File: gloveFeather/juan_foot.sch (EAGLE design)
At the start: 9 parts

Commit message: pcb for nano almost ready
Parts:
- removed FLEXPOWER, LCDSERIAL: (no value), SparkFun-Connectors:CONN_02
- removed RIGHTFLEX: (no value), SparkFun-Connectors:CONN_06LOCK
- added J1: (no value), SparkFun-Connectors:CONN_08"
- added LCD: (no value), SparkFun-Connectors:CONN_03
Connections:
- net 3V: now also J1.8; no longer FLEXPOWER.1, U$1.3.3V
- net GND: now also J1.7, LCD.3; no longer FLEXPOWER.2
- net PINKYFLEX: now also J1.5; no longer RIGHTFLEX.5
- net PINKYSIDE: now also J1.6, U$1.D3; no longer RIGHTFLEX.6, U$1.D2
- net RINGFLEX: now also J1.3; no longer RIGHTFLEX.3
- net RINGSIDE: now also J1.4, U$1.D2; no longer RIGHTFLEX.4, U$1.D3
- net SCL: now also J1.2; no longer RIGHTFLEX.2
- net SDA: now also J1.1; no longer RIGHTFLEX.1
- net SRX: now also LCD.1; no longer LCDSERIAL.2
- net STX: now also LCD.2; no longer LCDSERIAL.1
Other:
- moved on the sheet: SPEAKER
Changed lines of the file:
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@@
 <part name="U$1" library="Arduino-clone" deviceset="NANO" device=""/>
 <part name="LEFTFLEX" library="SparkFun-Connectors" deviceset="CONN_08" device="&quot;"/>
-<part name="RIGHTFLEX" library="SparkFun-Connectors" deviceset="CONN_06" device="LOCK"/>
-<part name="FLEXPOWER" library="SparkFun-Connectors" deviceset="CONN_02" device=""/>
 <part name="BAT" library="SparkFun-Connectors" deviceset="CONN_04" device=""/>
-<part name="LCDSERIAL" library="SparkFun-Connectors" deviceset="CONN_02" device=""/>
+<part name="J1" library="SparkFun-Connectors" deviceset="CONN_08" device="&quot;"/>
+<part name="LCD" library="SparkFun-Connectors" deviceset="CONN_03" device=""/>
 </parts>
 <sheets>
@@
 <instance part="GROUND" gate="G$1" x="-119.38" y="119.38"/>
 <instance part="VOLTAGE" gate="G$1" x="-73.66" y="119.38" rot="MR0"/>
-<instance part="SPEAKER" gate="G$1" x="86.36" y="17.78" rot="MR0"/>
+<instance part="SPEAKER" gate="G$1" x="81.28" y="17.78" rot="MR0"/>
 <instance part="U$1" gate="G$1" x="25.4" y="35.56"/>
 <instance part="LEFTFLEX" gate="G$1" x="-48.26" y="-5.08"/>
-<instance part="RIGHTFLEX" gate="G$1" x="-48.26" y="27.94"/>
-<instance part="FLEXPOWER" gate="G$1" x="-50.8" y="48.26"/>
 <instance part="BAT" gate="G$1" x="-119.38" y="73.66"/>
-<instance part="LCDSERIAL" gate="G$1" x="83.82" y="43.18" rot="MR0"/>
+<instance part="J1" gate="G$1" x="-48.26" y="27.94"/>
+<instance part="LCD" gate="J$1" x="48.26" y="-7.62" rot="R180"/>
 </instances>
 <busses>
@@
 <segment>
 <pinref part="SPEAKER" gate="G$1" pin="3"/>
-<wire x1="81.28" y1="20.32" x2="73.66" y2="20.32" width="0.1524" layer="91"/>
-<label x="73.66" y="20.32" size="1.778" layer="95"/>
-</segment>
-<segment>
-<pinref part="U$1" gate="G$1" pin="3.3V"/>
-<wire x1="2.54" y1="48.26" x2="-2.54" y2="48.26" width="0.1524" layer="91"/>
-<label x="-2.54" y="48.26" size="1.778" layer="95"/>
-</segment>
-<segment>
-<pinref part="FLEXPOWER" gate="G$1" pin="1"/>
+<wire x1="76.2" y1="20.32" x2="68.58" y2="20.32" width="0.1524" layer="91"/>
+<label x="68.58" y="20.32" size="1.778" layer="95"/>
+</segment>
+<segment>
 <wire x1="-43.18" y1="48.26" x2="-35.56" y2="48.26" width="0.1524" layer="91"/>
 <label x="-38.1" y="48.26" size="1.778" layer="95"/>
@@
 <label x="-5.08" y="15.24" size="1.778" layer="95"/>
 </segment>
+<segment>
+<pinref part="J1" gate="G$1" pin="8"/>
+<wire x1="-43.18" y1="38.1" x2="-40.64" y2="38.1" width="0.1524" layer="91"/>
+<label x="-43.18" y="38.1" size="1.778" layer="95"/>
+</segment>
 </net>
 <net name="GND" class="0">
 <segment>
 <pinref part="SPEAKER" gate="G$1" pin="4"/>
-<wire x1="81.28" y1="22.86" x2="73.66" y2="22.86" width="0.1524" layer="91"/>
-<label x="73.66" y="22.86" size="1.778" layer="95"/>
+<wire x1="76.2" y1="22.86" x2="68.58" y2="22.86" width="0.1524" layer="91"/>
+<label x="68.58" y="22.86" size="1.778" layer="95"/>
 </segment>
 <segment>
@@
 </segment>
 <segment>
-<pinref part="FLEXPOWER" gate="G$1" pin="2"/>
 <wire x1="-43.18" y1="50.8" x2="-35.56" y2="50.8" width="0.1524" layer="91"/>
 <label x="-38.1" y="50.8" size="1.778" layer="95"/>
@@
 <label x="-111.76" y="73.66" size="1.778" layer="95"/>
 </segment>
+<segment>
+<pinref part="J1" gate="G$1" pin="7"/>
+<wire x1="-43.18" y1="35.56" x2="-40.64" y2="35.56" width="0.1524" layer="91"/>
+<label x="-43.18" y="35.56" size="1.778" layer="95"/>
+</segment>
+<segment>
+<pinref part="LCD" gate="J$1" pin="3"/>
+<wire x1="40.64" y1="-10.16" x2="38.1" y2="-10.16" width="0.1524" layer="91"/>
+<label x="35.56" y="-10.16" size="1.778" layer="95"/>
+</segment>
 </net>
 <net name="SOUT" class="0">
 <segment>
 <pinref part="SPEAKER" gate="G$1" pin="2"/>
-<wire x1="81.28" y1="17.78" x2="73.66" y2="17.78" width="0.1524" layer="91"/>
-<label x="73.66" y="17.78" size="1.778" layer="95"/>
+<wire x1="76.2" y1="17.78" x2="68.58" y2="17.78" width="0.1524" layer="91"/>
+<label x="68.58" y="17.78" size="1.778" layer="95"/>
 </segment>
 <segment>
@@
 <segment>
 <pinref part="SPEAKER" gate="G$1" pin="1"/>
-<wire x1="81.28" y1="15.24" x2="73.66" y2="15.24" width="0.1524" layer="91"/>
-<label x="73.66" y="15.24" size="1.778" layer="95"/>
+<wire x1="76.2" y1="15.24" x2="68.58" y2="15.24" width="0.1524" layer="91"/>
+<label x="68.58" y="15.24" size="1.778" layer="95"/>
 </segment>
 <segment>
@@
 <net name="SDA" class="0">
 <segment>
-<pinref part="RIGHTFLEX" gate="G$1" pin="1"/>
-<wire x1="-43.18" y1="22.86" x2="-35.56" y2="22.86" width="0.1524" layer="91"/>
-<label x="-38.1" y="22.86" size="1.778" layer="95"/>
-</segment>
-<segment>
 <pinref part="U$1" gate="G$1" pin="A4"/>
 <wire x1="2.54" y1="33.02" x2="0" y2="33.02" width="0.1524" layer="91"/>
 <label x="-2.54" y="33.02" size="1.778" layer="95"/>
 </segment>
+<segment>
+<pinref part="J1" gate="G$1" pin="1"/>
+<wire x1="-43.18" y1="20.32" x2="-40.64" y2="20.32" width="0.1524" layer="91"/>
+<label x="-43.18" y="20.32" size="1.778" layer="95"/>
+</segment>
 </net>
 <net name="SCL" class="0">
-<segment>
-<pinref part="RIGHTFLEX" gate="G$1" pin="2"/>
-<wire x1="-43.18" y1="25.4" x2="-35.56" y2="25.4" width="0.1524" layer="91"/>
-<label x="-38.1" y="25.4" size="1.778" layer="95"/>
-</segment>
 <segment>
 <pinref part="U$1" gate="G$1" pin="A5"/>
@@
 <label x="-2.54" y="30.48" size="1.778" layer="95"/>
 </segment>
+<segment>
+<pinref part="J1" gate="G$1" pin="2"/>
+<wire x1="-43.18" y1="22.86" x2="-40.64" y2="22.86" width="0.1524" layer="91"/>
+<label x="-43.18" y="22.86" size="1.778" layer="95"/>
+</segment>
 </net>
 <net name="RINGFLEX" class="0">
-<segment>
-<pinref part="RIGHTFLEX" gate="G$1" pin="3"/>
-<wire x1="-43.18" y1="27.94" x2="-35.56" y2="27.94" width="0.1524" layer="91"/>
-<label x="-38.1" y="27.94" size="1.778" layer="95"/>
-</segment>
 <segment>
 <pinref part="U$1" gate="G$1" pin="A6"/>
@@
 <label x="-12.7" y="27.94" size="1.778" layer="95"/>
 </segment>
+<segment>
+<pinref part="J1" gate="G$1" pin="3"/>
+<wire x1="-43.18" y1="25.4" x2="-40.64" y2="25.4" width="0.1524" layer="91"/>
+<label x="-43.18" y="25.4" size="1.778" layer="95"/>
+</segment>
 </net>
 <net name="RINGSIDE" class="0">
 <segment>
-<pinref part="RIGHTFLEX" gate="G$1" pin="4"/>
-<wire x1="-43.18" y1="30.48" x2="-35.56" y2="30.48" width="0.1524" layer="91"/>
-<label x="-38.1" y="30.48" size="1.778" layer="95"/>
+<pinref part="J1" gate="G$1" pin="4"/>
+<wire x1="-43.18" y1="27.94" x2="-40.64" y2="27.94" width="0.1524" layer="91"/>
+<label x="-43.18" y="27.94" size="1.778" layer="95"/>
+</segment>
+<segment>
+<pinref part="U$1" gate="G$1" pin="D2"/>
+<wire x1="35.56" y1="25.4" x2="38.1" y2="25.4" width="0.1524" layer="91"/>
+<label x="35.56" y="25.4" size="1.778" layer="95"/>
+</segment>
+</net>
+<net name="PINKYFLEX" class="0">
+<segment>
+<pinref part="U$1" gate="G$1" pin="A7"/>
+<wire x1="2.54" y1="25.4" x2="-2.54" y2="25.4" width="0.1524" layer="91"/>
+<label x="-12.7" y="25.4" size="1.778" layer="95"/>
+</segment>
+<segment>
+<pinref part="J1" gate="G$1" pin="5"/>
+<wire x1="-43.18" y1="30.48" x2="-40.64" y2="30.48" width="0.1524" layer="91"/>
+<label x="-43.18" y="30.48" size="1.778" layer="95"/>
+</segment>
+</net>
+<net name="PINKYSIDE" class="0">
+<segment>
+<pinref part="J1" gate="G$1" pin="6"/>
+<wire x1="-43.18" y1="33.02" x2="-40.64" y2="33.02" width="0.1524" layer="91"/>
+<label x="-43.18" y="33.02" size="1.778" layer="95"/>
 </segment>
 <segment>
@@
 <wire x1="35.56" y1="27.94" x2="38.1" y2="27.94" width="0.1524" layer="91"/>
 <label x="35.56" y="27.94" size="1.778" layer="95"/>
-</segment>
-</net>
-<net name="PINKYFLEX" class="0">
-<segment>
-<pinref part="RIGHTFLEX" gate="G$1" pin="5"/>
-<wire x1="-43.18" y1="33.02" x2="-35.56" y2="33.02" width="0.1524" layer="91"/>
-<label x="-38.1" y="33.02" size="1.778" layer="95"/>
-</segment>
-<segment>
-<pinref part="U$1" gate="G$1" pin="A7"/>
-<wire x1="2.54" y1="25.4" x2="-2.54" y2="25.4" width="0.1524" layer="91"/>
-<label x="-12.7" y="25.4" size="1.778" layer="95"/>
-</segment>
-</net>
-<net name="PINKYSIDE" class="0">
-<segment>
-<pinref part="RIGHTFLEX" gate="G$1" pin="6"/>
-<wire x1="-43.18" y1="35.56" x2="-35.56" y2="35.56" width="0.1524" layer="91"/>
-<label x="-38.1" y="35.56" size="1.778" layer="95"/>
-</segment>
-<segment>
-<pinref part="U$1" gate="G$1" pin="D2"/>
-<wire x1="35.56" y1="25.4" x2="38.1" y2="25.4" width="0.1524" layer="91"/>
-<label x="35.56" y="25.4" size="1.778" layer="95"/>
 </segment>
 </net>
@@
 <net name="SRX" class="0">
 <segment>
-<pinref part="LCDSERIAL" gate="G$1" pin="2"/>
-<wire x1="76.2" y1="45.72" x2="71.12" y2="45.72" width="0.1524" layer="91"/>
-<label x="68.58" y="45.72" size="1.778" layer="95"/>
-</segment>
-<segment>
 <pinref part="U$1" gate="G$1" pin="D6"/>
 <wire x1="35.56" y1="35.56" x2="40.64" y2="35.56" width="0.1524" layer="91"/>
 <label x="38.1" y="35.56" size="1.778" layer="95"/>
 </segment>
+<segment>
+<pinref part="LCD" gate="J$1" pin="1"/>
+<wire x1="40.64" y1="-5.08" x2="38.1" y2="-5.08" width="0.1524" layer="91"/>
+<label x="35.56" y="-5.08" size="1.778" layer="95"/>
+</segment>
 </net>
 <net name="STX" class="0">
-<segment>
-<pinref part="LCDSERIAL" gate="G$1" pin="1"/>
-<wire x1="76.2" y1="43.18" x2="71.12" y2="43.18" width="0.1524" layer="91"/>
-<label x="68.58" y="43.18" size="1.778" layer="95"/>
-</segment>
 <segment>
 <pinref part="U$1" gate="G$1" pin="D5"/>
@@
 <label x="38.1" y="33.02" size="1.778" layer="95"/>
 </segment>
-</net>
+<segment>
+<pinref part="LCD" gate="J$1" pin="2"/>
+<wire x1="40.64" y1="-7.62" x2="38.1" y2="-7.62" width="0.1524" layer="91"/>
+<label x="35.56" y="-7.62" size="1.778" layer="95"/>
+</segment>
+</net>

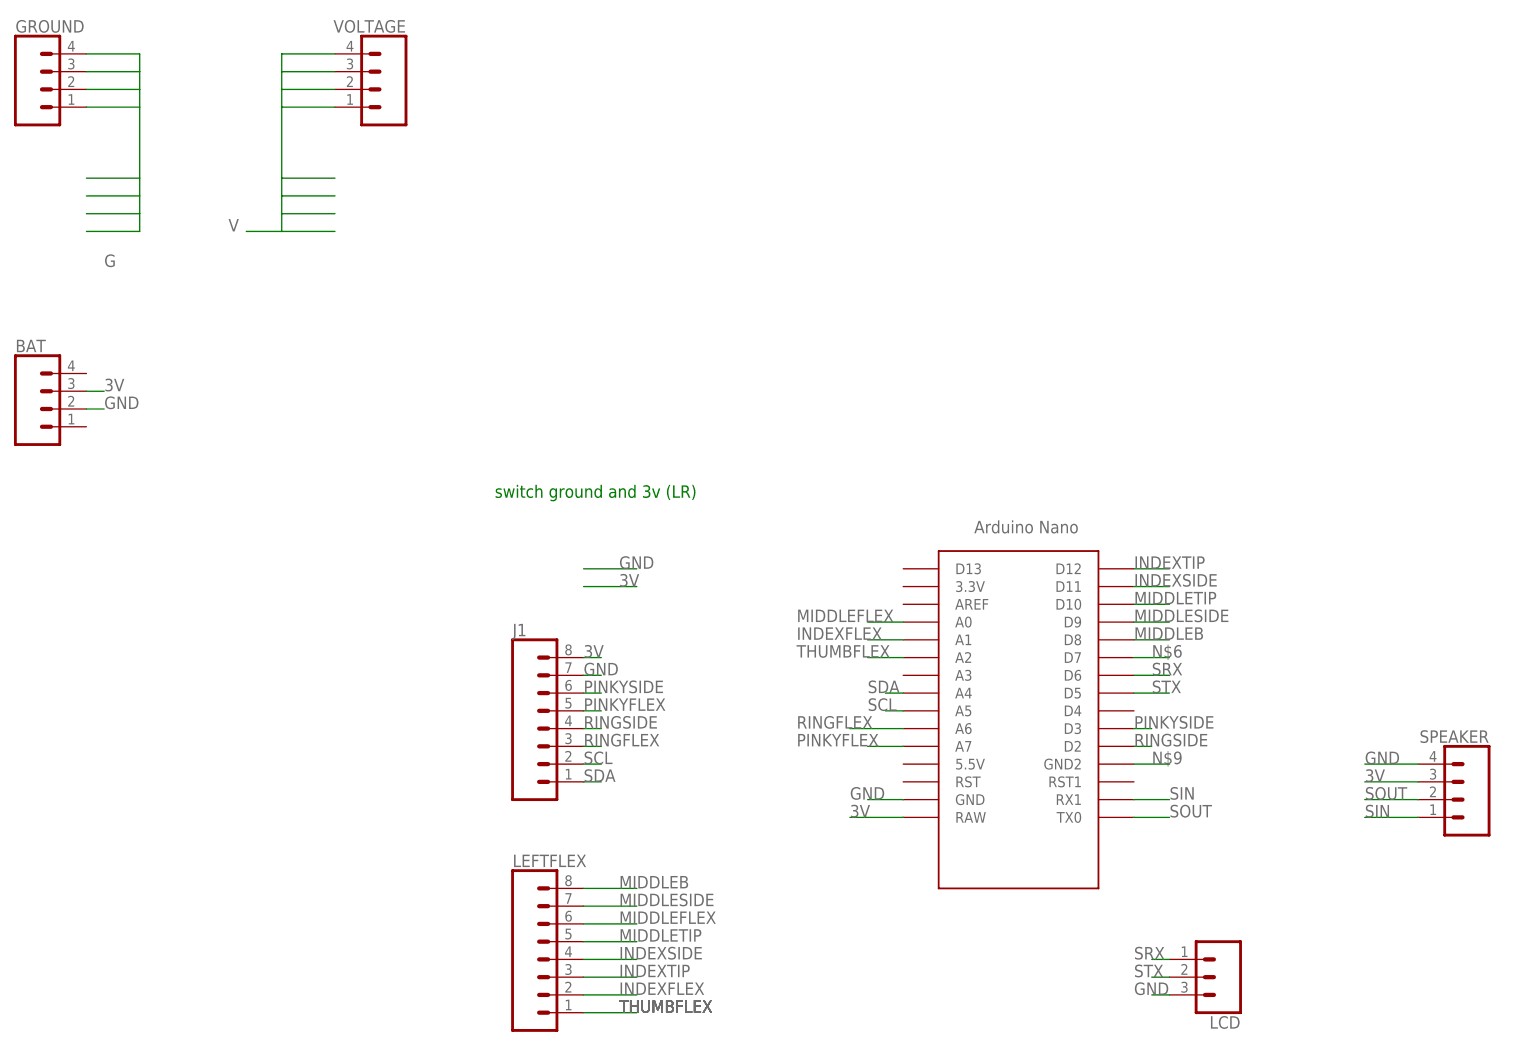
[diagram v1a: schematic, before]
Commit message: pcb updated with new connections. Added 3V plane
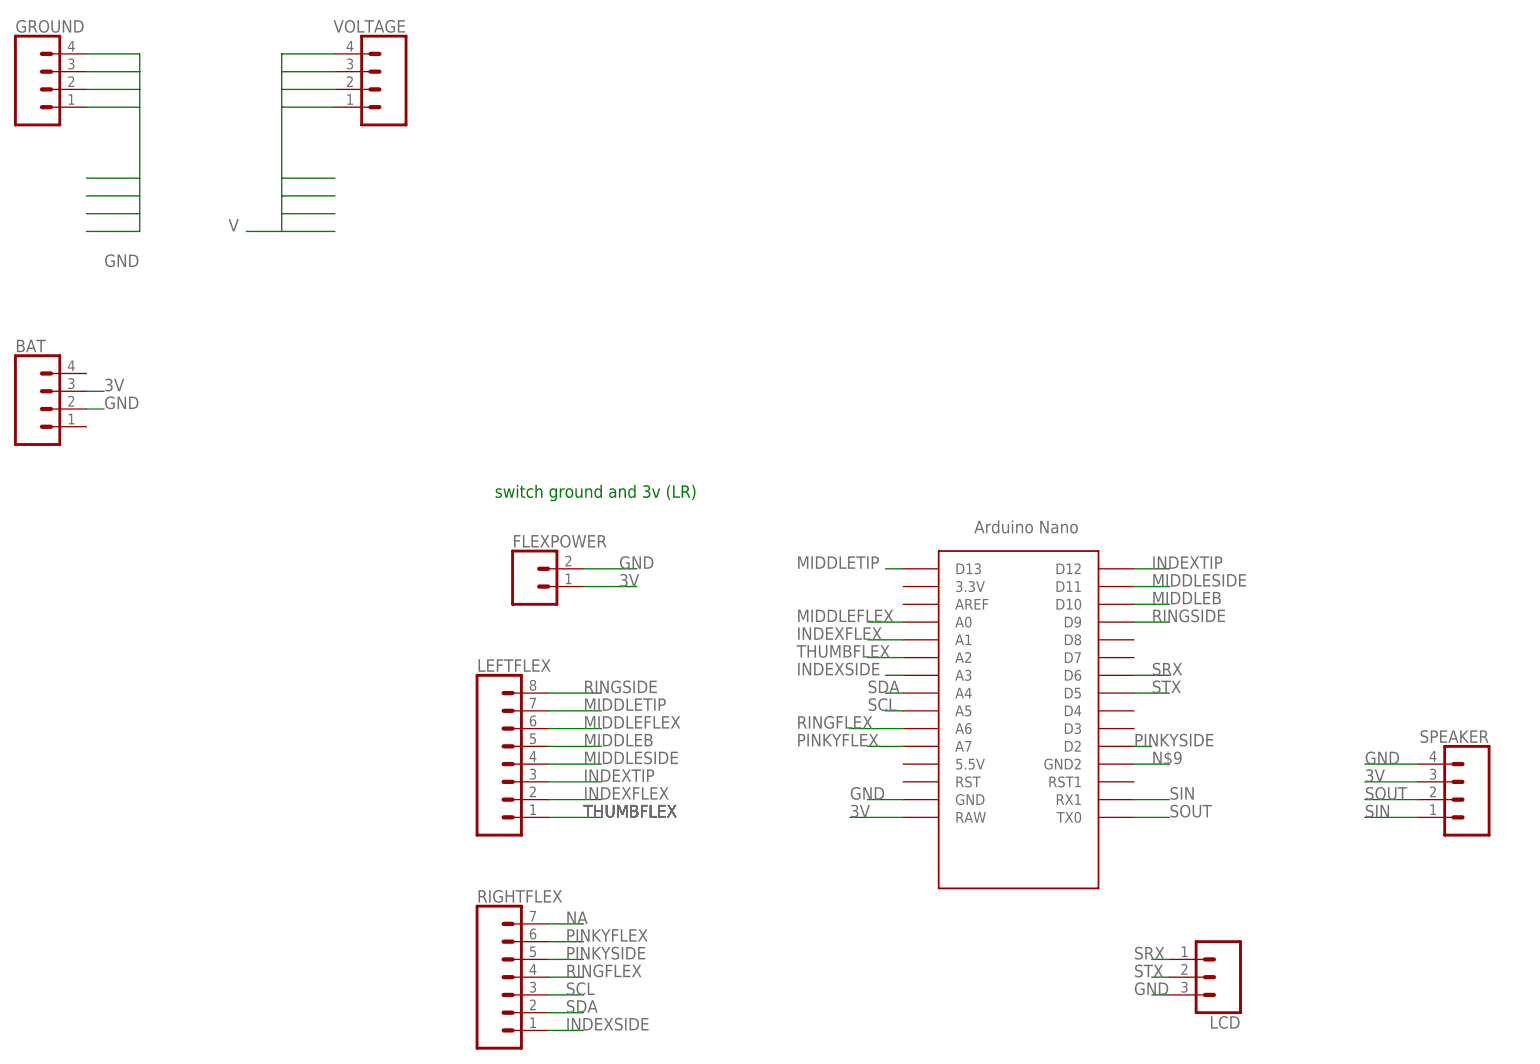
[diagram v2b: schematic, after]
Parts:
- removed J1: (no value), SparkFun-Connectors:CONN_08"
- added FLEXPOWER: (no value), SparkFun-Connectors:CONN_02
- added RIGHTFLEX: (no value), SparkFun-Connectors:CONN_07
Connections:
- removed net G: GROUND.1, GROUND.2, GROUND.3, GROUND.4
- removed net N$6: U$1.D7
- new net NA: RIGHTFLEX.7
- net 3V: now also FLEXPOWER.1; no longer J1.8
- net GND: now also FLEXPOWER.2, GROUND.1, GROUND.2, GROUND.3, GROUND.4; no longer J1.7
- net INDEXSIDE: now also RIGHTFLEX.1, U$1.A3; no longer LEFTFLEX.4, U$1.D11
- net MIDDLEB: now also LEFTFLEX.5, U$1.D10; no longer LEFTFLEX.8, U$1.D8
- net MIDDLESIDE: now also LEFTFLEX.4, U$1.D11; no longer LEFTFLEX.7, U$1.D9
- net MIDDLETIP: now also LEFTFLEX.7, U$1.D13; no longer LEFTFLEX.5, U$1.D10
- net PINKYFLEX: now also RIGHTFLEX.6; no longer J1.5
- net PINKYSIDE: now also RIGHTFLEX.5, U$1.D2; no longer J1.6, U$1.D3
- net RINGFLEX: now also RIGHTFLEX.4; no longer J1.3
- net RINGSIDE: now also LEFTFLEX.8, U$1.D9; no longer J1.4, U$1.D2
- net SCL: now also RIGHTFLEX.3; no longer J1.2
- net SDA: now also RIGHTFLEX.2; no longer J1.1
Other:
- moved on the sheet: LEFTFLEX

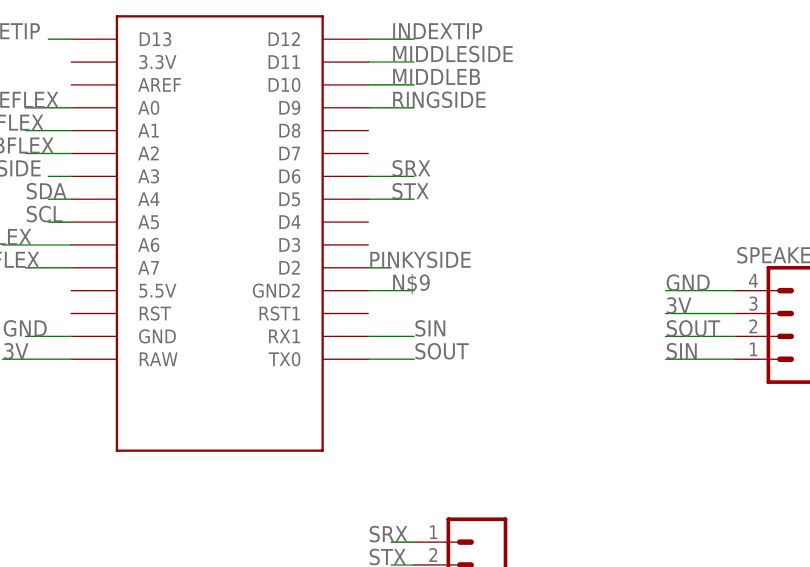
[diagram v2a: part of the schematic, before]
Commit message: finished glove pcb and speaker pcb
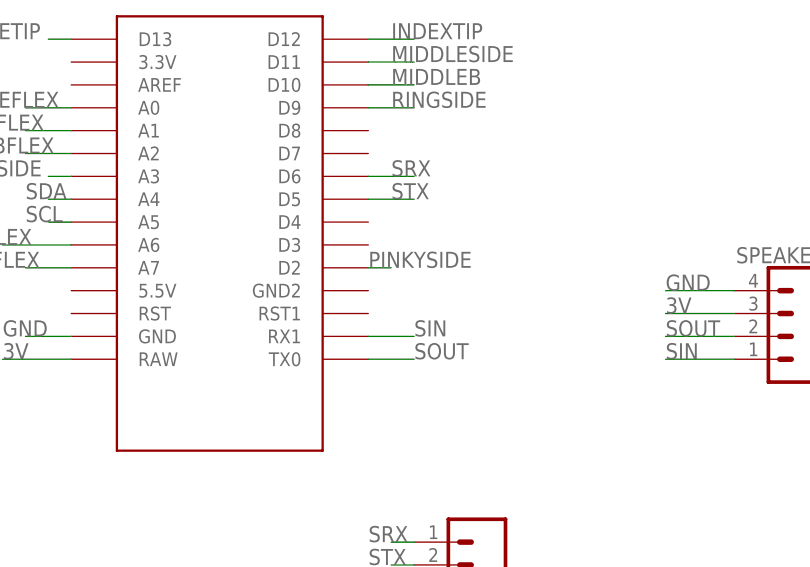
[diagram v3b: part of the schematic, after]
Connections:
- removed net N$9: U$1.GND2
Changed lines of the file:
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@@
-</segment>
-</net>
-<net name="N$9" class="0">
-<segment>
-<pinref part="U$1" gate="G$1" pin="GND2"/>
-<wire x1="35.56" y1="22.86" x2="40.64" y2="22.86" width="0.1524" layer="91"/>
-<label x="38.1" y="22.86" size="1.778" layer="95"/>
 </segment>
 </net>

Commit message: final pcb
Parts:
- removed GROUND, VOLTAGE: (no value), SparkFun-Connectors:CONN_04
- removed U$1: NANO, Arduino-clone:NANO
- added J1: (no value), SparkFun-Connectors:CONN_01
- added LEFTFEATHER, RIGHTFEATHER: (no value), SparkFun-Connectors:CONN_15
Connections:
- removed net V: VOLTAGE.1, VOLTAGE.2, VOLTAGE.3, VOLTAGE.4
- new net 5V: LEFTFEATHER.4
- new net D3: RIGHTFEATHER.6
- new net D4: RIGHTFEATHER.7
- new net D7: RIGHTFEATHER.10
- new net N$13: LEFTFEATHER.13
- new net RST: LEFTFEATHER.3, RIGHTFEATHER.3
- new net VIN: BAT.3, LEFTFEATHER.1
- net 3V: now also J1.1, LEFTFEATHER.14; no longer BAT.3, U$1.RAW
- net GND: now also LEFTFEATHER.2, RIGHTFEATHER.4; no longer GROUND.1, GROUND.2, GROUND.3, GROUND.4, U$1.GND
- net INDEXFLEX: now also LEFTFEATHER.11; no longer U$1.A1
- net INDEXSIDE: now also LEFTFEATHER.9; no longer U$1.A3
- net INDEXTIP: now also RIGHTFEATHER.14; no longer U$1.D12
- net MIDDLEB: now also RIGHTFEATHER.12; no longer U$1.D10
- net MIDDLEFLEX: now also LEFTFEATHER.12; no longer U$1.A0
- net MIDDLESIDE: now also RIGHTFEATHER.13; no longer U$1.D11
- net MIDDLETIP: now also LEFTFEATHER.15; no longer U$1.D13
- net PINKYFLEX: now also LEFTFEATHER.5; no longer U$1.A7
- net PINKYSIDE: now also RIGHTFEATHER.15; no longer U$1.D2
- net RINGFLEX: now also LEFTFEATHER.6; no longer U$1.A6
- net RINGSIDE: now also RIGHTFEATHER.11; no longer U$1.D9
- net SCL: now also LEFTFEATHER.7; no longer U$1.A5
- net SDA: now also LEFTFEATHER.8; no longer U$1.A4
- net SIN: now also RIGHTFEATHER.2; no longer U$1.RX1
- net SOUT: now also RIGHTFEATHER.1; no longer U$1.TX0
- net SRX: now also RIGHTFEATHER.9; no longer U$1.D6
- net STX: now also RIGHTFEATHER.8; no longer U$1.D5
- net THUMBFLEX: now also LEFTFEATHER.10; no longer U$1.A2
